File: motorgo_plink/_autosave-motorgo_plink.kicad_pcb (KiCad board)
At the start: 4 copper layers, 80.5 x 64.5 mm, 141 parts, among them J1 USB4520-03-0-A_REVA, J10 Conn_01x02_Pin, J13 I2C_STANDARDQWIIC, J14 BM05B-SRSS-TB_LF__SN_, J15 I2C_STANDARDQWIIC, J16 BM05B-SRSS-TB_LF__SN_, J17 I2C_STANDARDQWIIC, J18 BM05B-SRSS-TB_LF__SN_, J19 I2C_STANDARDQWIIC, J20 BM05B-SRSS-TB_LF__SN_, J22 Conn_01x02_Pin, J23 Conn_01x06_Pin, J4 Conn_02x20_Odd_Even, J5 Conn_02x20_Odd_Even, J6 Conn_01x02_Pin, J7 USB4520-03-0-A_REVA, J8 Conn_01x02_Pin, Q1 SI2323, U1 ESP32-S3-WROOM-1, U10 LIS3MDLTR, U11 LSM6DS3TR, U2 USBLC6-2P6, U3 DRV8874PWPR, U4 DRV8874PWPR, U5 DRV8874PWPR, U6 TPS54620RHLR, U7 HUSB238_002DD, U8 AMS1117-3.3, U9 DRV8874PWPR

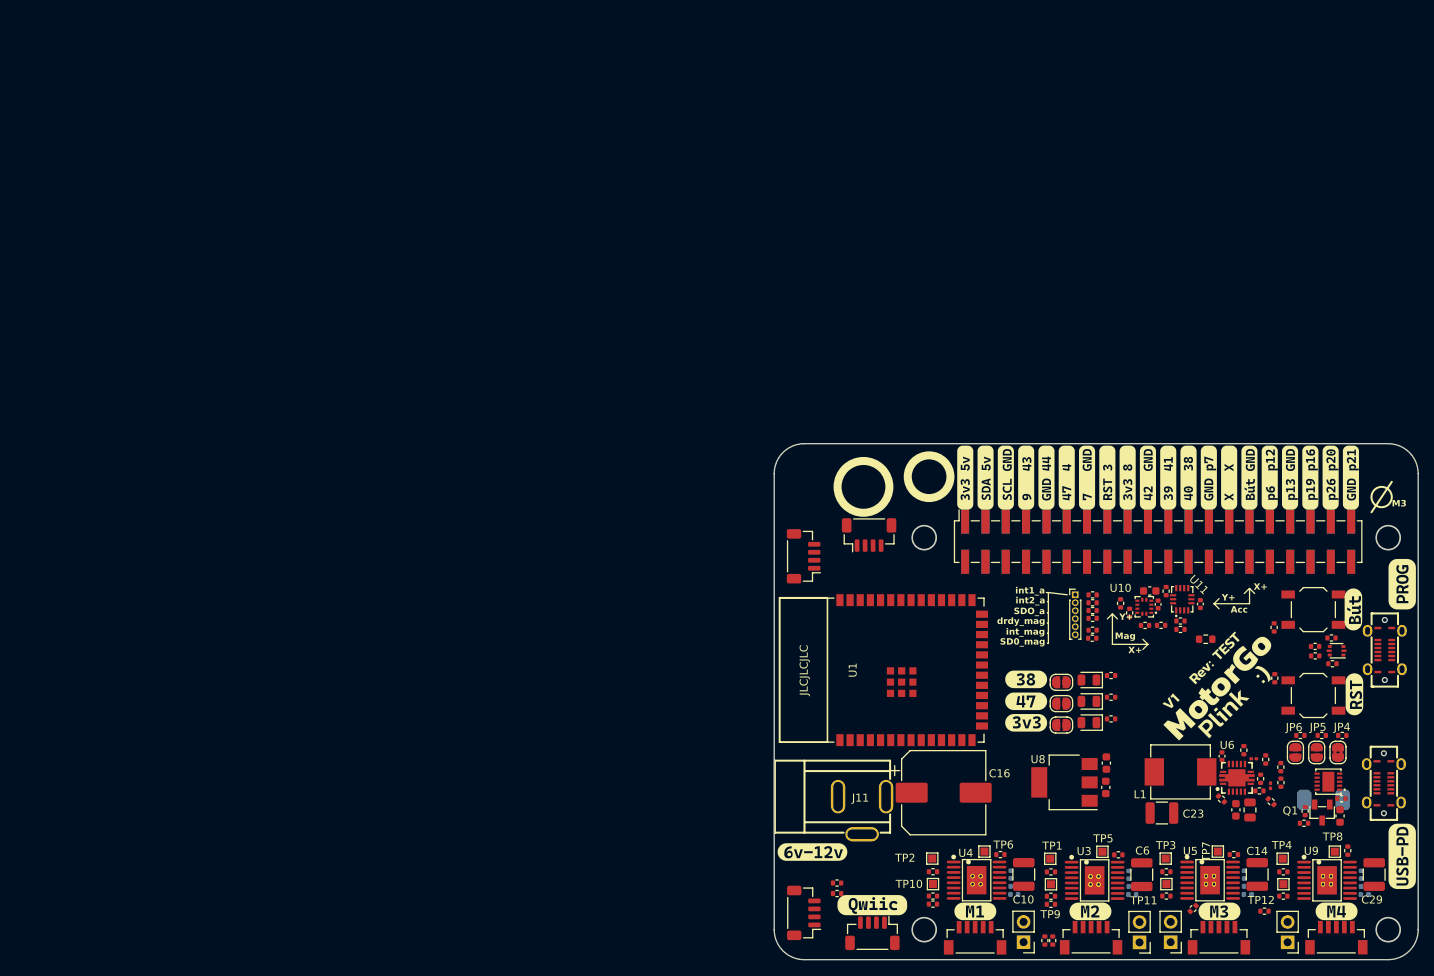
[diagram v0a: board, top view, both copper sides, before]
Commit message: wip schematic edits to account for buck reg design
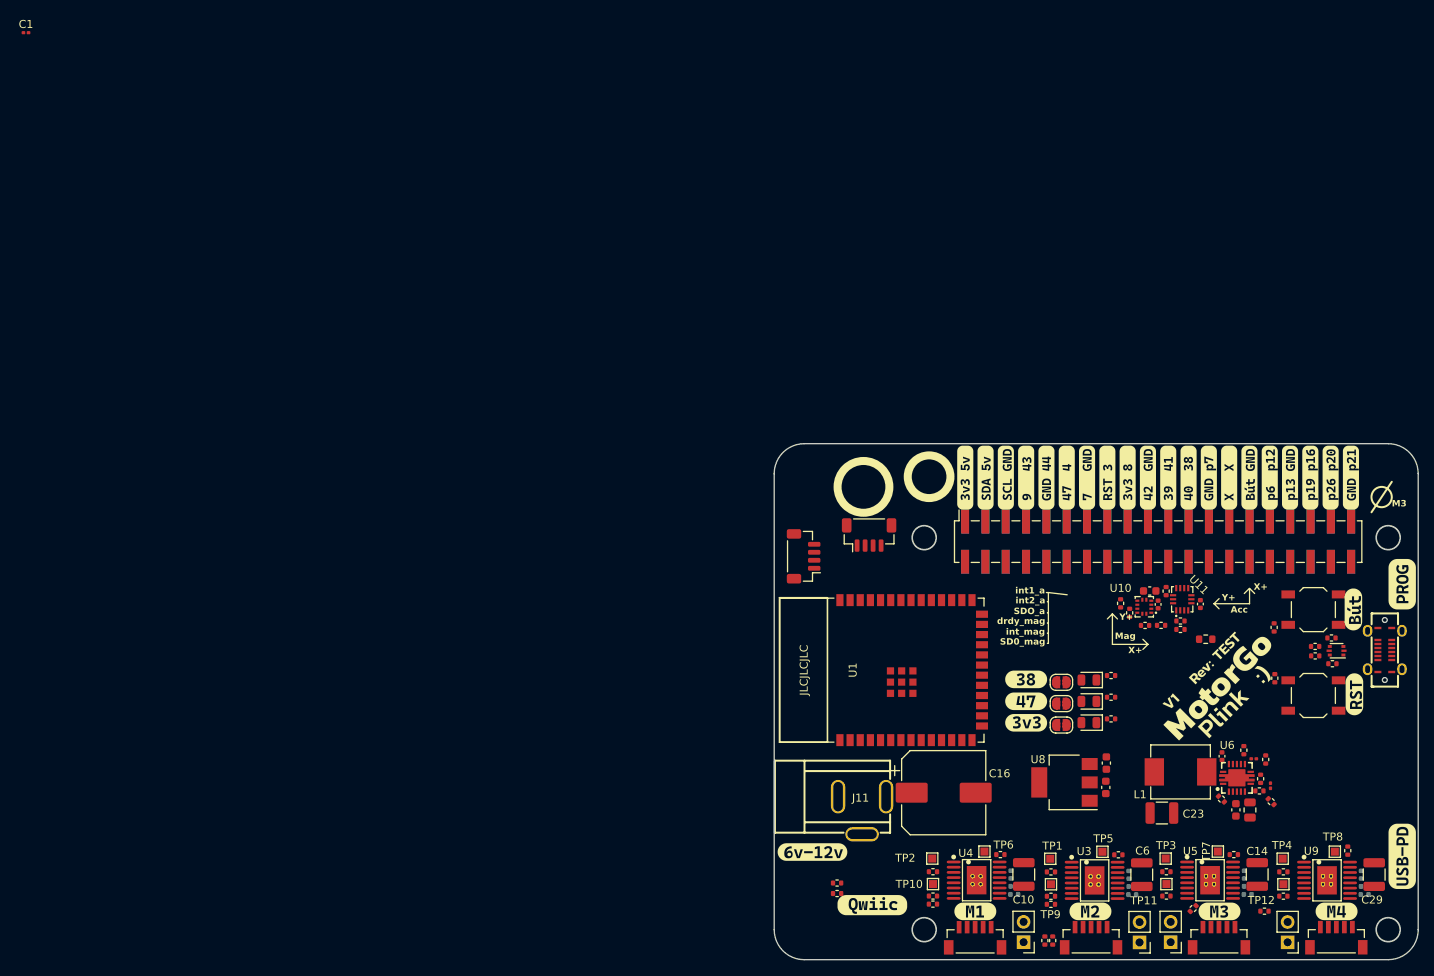
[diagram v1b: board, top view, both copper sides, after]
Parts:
- removed C21: 1uF, Capacitor_SMD:C_0603_1608Metric
- removed D4: 20V 5A, LCSC_parts:D_SMB_LCSC_C5366311
- removed J17, J19: I2C_STANDARDQWIIC, Connector_JST:JST_SH_BM04B-SRSS-TB_1x04-1MP_P1.00mm_Vertical
- removed J23: Conn_01x06_Pin, Connector_PinHeader_1.00mm:PinHeader_1x06_P1.00mm_Vertical
- removed J7: USB4520-03-0-A_REVA, mg_mini_v1r3:USB-C-SMD_TYPEC-303-ACP16
- removed JP4: SolderJumper_2_Bridged, Jumper:SolderJumper-2_P1.3mm_Bridged2Bar_RoundedPad1.0x1.5mm
- removed JP5, JP6: SolderJumper_2_Open, Jumper:SolderJumper-2_P1.3mm_Open_RoundedPad1.0x1.5mm
- removed Q1: SI2323, LCSC_parts:SI2323_SOT-23-3_L2.9-W1.3-P0.95-LS2.4-BR
- removed R20: 10R 1%, Resistor_SMD:R_0402_1005Metric
- removed R21, R22, R40, R41, R42, R43, R44, R45: DNP, Resistor_SMD:R_0402_1005Metric
- removed R23: 5.1K, Resistor_SMD:R_0402_1005Metric
- removed R26: 49.9K, Resistor_SMD:R_0402_1005Metric
- removed R27: 10K, Resistor_SMD:R_0402_1005Metric
- removed R28: 14K, Resistor_SMD:R_0402_1005Metric
- removed R29: 10.5K, Resistor_SMD:R_0402_1005Metric
- removed U7: HUSB238_002DD, LCSC_parts:DFN-10_L3.0-W3.0-P0.50-BL-EP2.5
- added C1: 43pF 0Ohm, Capacitor_SMD:C_0201_0603Metric, F.Cu at (0.72, 0.38)
- R19: value 3.4k -> 3.92k
- R24: value 52.3k -> 53.6k
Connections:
- J14 pad 1: m1_enc_cs -> (no net)
- J14 pad 2: enc_scl -> (no net)
- J14 pad 3: enc_sda -> (no net)
- J16 pad 1: m2_enc_cs -> (no net)
- J16 pad 2: enc_scl -> /connectors.enc_scl
- J16 pad 3: enc_sda -> /connectors.enc_sda
- J18 pad 1: m3_enc_cs -> (no net)
- J18 pad 2: enc_scl -> /connectors.enc_scl
- J18 pad 3: enc_sda -> /connectors.enc_sda
- J2 pad 2: boot -> (no net)
- J20 pad 1: m4_enc_cs -> (no net)
- J20 pad 2: enc_scl -> /connectors.enc_scl
- J20 pad 3: enc_sda -> /connectors.enc_sda
- J4 pad 15: Reset -> reset
- J4 pad 29: boot -> /Boot
- J5 pad 16: Reset -> reset
- JP1 pad 2: gpio47 -> gpio42
- JP2 pad 2: gpio38 -> (no net)
- R32 pad 2: enc_scl -> /connectors.enc_scl
- R33 pad 2: enc_sda -> /connectors.enc_sda
- R38 pad 2: hidden_sda -> (no net)
- R39 pad 2: hidden_scl -> (no net)
- R46 pad 1: /IMU 6 + 3/SDO_mag -> (no net)
- R47 pad 1: /IMU 6 + 3/SDO_mag -> Net-(U10-SD0/SA1)
- R48 pad 1: /IMU 6 + 3/SDO_acc -> (no net)
- R49 pad 1: /IMU 6 + 3/SDO_acc -> Net-(U11-SDO/SA0)
- R8 pad 2: boot -> /Boot
- U1 pad 17: m3_enc_cs -> /connectors.enc3.cs
- U1 pad 20: m4_enc_cs -> /connectors.enc4.cs
- U1 pad 21: hidden_sda -> (no net)
- U1 pad 22: hidden_scl -> (no net)
- U1 pad 23: gpio38 -> /gpio21
- U1 pad 24: gpio41 -> gpio47
- U1 pad 25: gpio42 -> (no net)
- U1 pad 27: boot -> /Boot
- U1 pad 28: gpio4 -> (no net)
- U1 pad 29: gpio7 -> (no net)
- U1 pad 30: gpio3 -> (no net)
- U1 pad 31: gpio8 -> gpio38
- U1 pad 34: gpio44 -> gpio41
- U1 pad 35: gpio47 -> gpio42
- U1 pad 36: gpio43 -> gpio44
- U1 pad 37: gpio9 -> gpio43
- U1 pad 4: m2_enc_cs -> /connectors.enc2.cs
- U1 pad 5: m1_enc_cs -> /connectors.enc1.cs
- U1 pad 6: enc_sda -> /connectors.enc_sda
- U1 pad 7: enc_scl -> /connectors.enc_scl
- U10 pad 1: hidden_scl -> /IMU 6 + 3/SCL_acc
- U10 pad 11: hidden_sda -> /IMU 6 + 3/SDA_acc
- U10 pad 7: /IMU 6 + 3/INT_mag -> (no net)
- U10 pad 8: /IMU 6 + 3/DRDY_mag -> (no net)
- U10 pad 9: /IMU 6 + 3/SDO_mag -> Net-(U10-SD0/SA1)
- U11 pad 1: /IMU 6 + 3/SDO_acc -> Net-(U11-SDO/SA0)
- U11 pad 13: hidden_sda -> /IMU 6 + 3/SDA_acc
- U11 pad 14: hidden_scl -> /IMU 6 + 3/SCL_acc
- U11 pad 2: /IMU 6 + 3/SDX_acc -> (no net)
- U11 pad 3: /IMU 6 + 3/SCX_acc -> (no net)
- U11 pad 4: /IMU 6 + 3/INT1_acc -> (no net)
- U11 pad 9: /IMU 6 + 3/INT2_acc -> (no net)
